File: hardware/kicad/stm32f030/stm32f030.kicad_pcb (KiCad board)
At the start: 2 copper layers, 72.4 x 50.2 mm, 91 parts, among them IC1 AT24CS02-SSHM, K1 RELAY_1RT, K2 RELAY_1RT, P1 5VIN, P10 SWD, P2 LOOP1, P3 LOOP2, P4 RELAY OUT 1, P5 TTL OUT 1, P6 RELAY OUT 2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

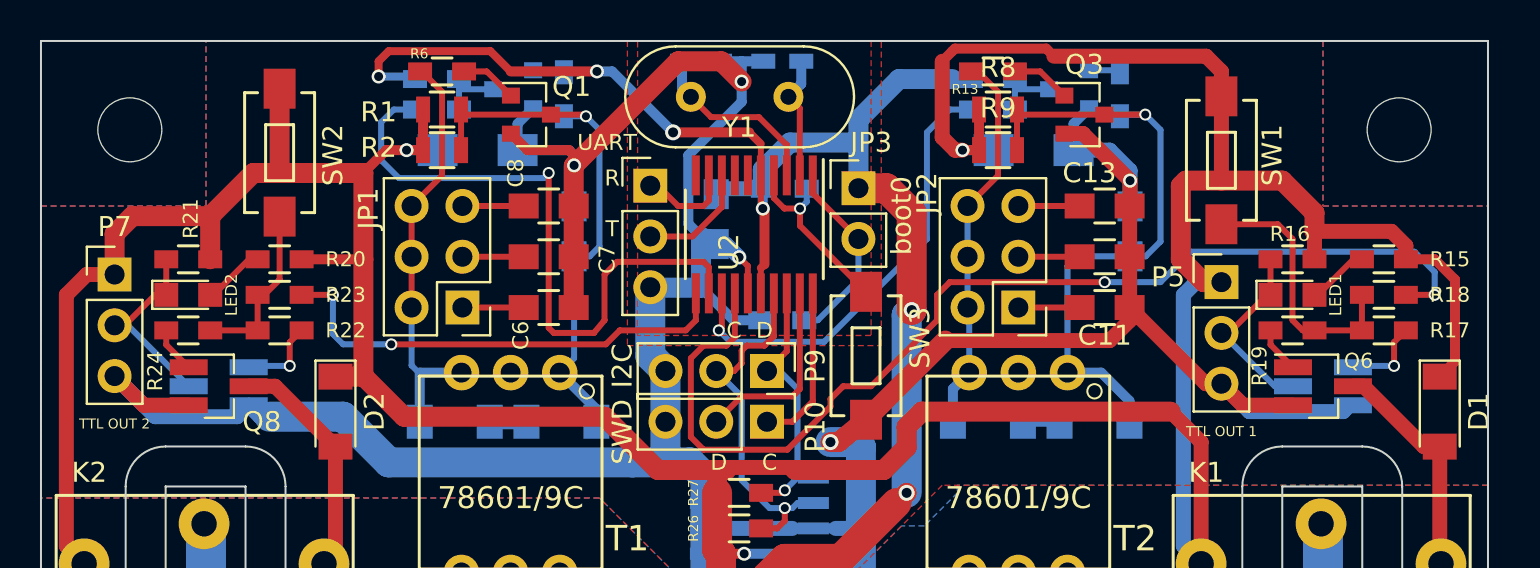
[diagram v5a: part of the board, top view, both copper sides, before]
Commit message: stm32f030 PCB text fixes
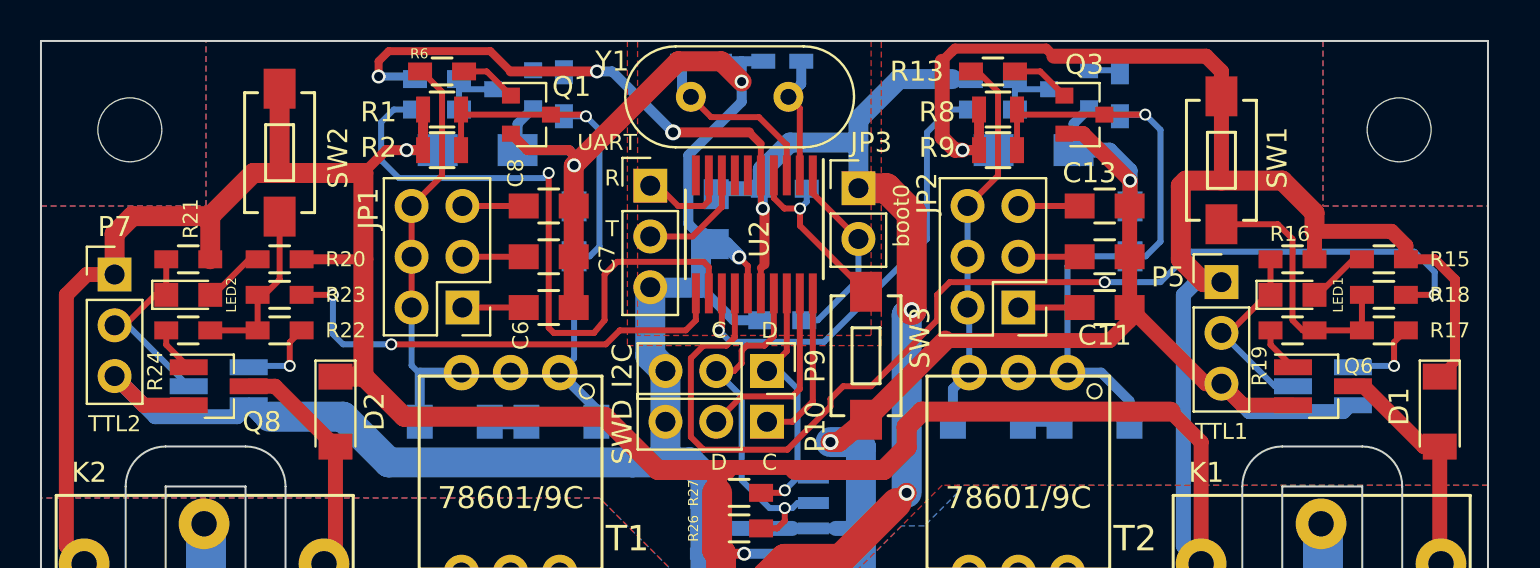
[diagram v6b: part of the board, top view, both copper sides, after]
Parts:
- P5: value TTL OUT 1 -> TTL1
- P7: value TTL OUT 2 -> TTL2
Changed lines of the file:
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@@
     (links 174)
     (no_connects 0)
-    (area 53.924999 112.979999 126.415001 163.245001)
+    (area 39.140001 103.98 131.527143 168.054001)
     (thickness 1.6)
     (drawings 40)
@@
     (46 B.CrtYd user)
     (47 F.CrtYd user)
-    (48 B.Fab user hide)
-    (49 F.Fab user hide)
+    (48 B.Fab user)
+    (49 F.Fab user)
   )
   (setup
@@
     (tags "capacitor 1206")
     (attr smd)
-    (fp_text reference C4 (at 1.397 1.905) (layer B.SilkS)
+    (fp_text reference C4 (at 1.905 2.159) (layer B.SilkS)
       (effects (font (size 1 1) (thickness 0.15)) (justify mirror))
     )
@@
     (tags "capacitor 0805")
     (attr smd)
-    (fp_text reference C5 (at 0.127 1.651 90) (layer B.SilkS)
+    (fp_text reference C5 (at 0.127 1.905 90) (layer B.SilkS)
       (effects (font (size 1 1) (thickness 0.15)) (justify mirror))
     )
@@
     (tags "capacitor 1206")
     (attr smd)
-    (fp_text reference C9 (at 1.016 1.905) (layer B.SilkS)
+    (fp_text reference C9 (at 1.778 2.159) (layer B.SilkS)
       (effects (font (size 1 1) (thickness 0.15)) (justify mirror))
     )
@@
     (tags "capacitor 0603")
     (attr smd)
-    (fp_text reference C14 (at -2.667 1.27) (layer B.SilkS)
+    (fp_text reference C14 (at -3.429 0.254) (layer B.SilkS)
       (effects (font (size 1 1) (thickness 0.15)) (justify mirror))
     )
@@
     (tags "capacitor 0603")
     (attr smd)
-    (fp_text reference C15 (at -2.921 -1.27 180) (layer B.SilkS)
+    (fp_text reference C15 (at -3.429 -0.254 180) (layer B.SilkS)
       (effects (font (size 1 1) (thickness 0.15)) (justify mirror))
     )
@@
     (tags "LED led 0805 SMD smd SMT smt smdled SMDLED smtled SMTLED")
     (attr smd)
-    (fp_text reference LED1 (at 2.159 0 90) (layer F.SilkS)
-      (effects (font (size 0.6 0.6) (thickness 0.1)))
+    (fp_text reference LED1 (at 2.286 0 90) (layer F.SilkS)
+      (effects (font (size 0.5 0.5) (thickness 0.08)))
     )
     (fp_text value LED_Small (at 0 1.55) (layer F.Fab) hide
@@
     (attr smd)
     (fp_text reference LED2 (at 2.159 0 90) (layer F.SilkS)
-      (effects (font (size 0.6 0.6) (thickness 0.1)))
+      (effects (font (size 0.5 0.5) (thickness 0.08)))
     )
     (fp_text value LED_Small (at 0 1.55) (layer F.Fab) hide
@@
     (tags "resistor 0603")
     (attr smd)
-    (fp_text reference R3 (at 0.127 -1.397) (layer B.SilkS)
-      (effects (font (size 0.5 0.5) (thickness 0.1)) (justify mirror))
+    (fp_text reference R3 (at -2.921 -0.127) (layer B.SilkS)
+      (effects (font (size 0.8 0.8) (thickness 0.1)) (justify mirror))
     )
     (fp_text value 1k (at -4.953 0) (layer B.Fab) hide
@@
     (tags "resistor 0603")
     (attr smd)
-    (fp_text reference R4 (at -2.667 -0.127) (layer B.SilkS)
-      (effects (font (size 0.5 0.5) (thickness 0.1)) (justify mirror))
+    (fp_text reference R4 (at -2.921 -0.127) (layer B.SilkS)
+      (effects (font (size 0.8 0.8) (thickness 0.1)) (justify mirror))
     )
     (fp_text value 4.7k (at -5.588 -0.127) (layer B.Fab) hide
@@
     (tags "resistor 0603")
     (attr smd)
-    (fp_text reference R5 (at -0.127 1.397 90) (layer B.SilkS)
+    (fp_text reference R5 (at -0.127 1.651 90) (layer B.SilkS)
       (effects (font (size 0.8 0.8) (thickness 0.1)) (justify mirror))
     )
@@
     (tags "resistor 0603")
     (attr smd)
-    (fp_text reference R10 (at -2.794 -0.127 180) (layer B.SilkS)
-      (effects (font (size 0.5 0.5) (thickness 0.1)) (justify mirror))
+    (fp_text reference R10 (at -3.302 -0.127) (layer B.SilkS)
+      (effects (font (size 0.8 0.8) (thickness 0.1)) (justify mirror))
     )
     (fp_text value 1k (at -5.715 0.127) (layer B.Fab) hide
@@
     (tags "resistor 0603")
     (attr smd)
-    (fp_text reference R11 (at -2.794 -0.127 180) (layer B.SilkS)
-      (effects (font (size 0.5 0.5) (thickness 0.1)) (justify mirror))
+    (fp_text reference R11 (at -3.302 -0.127) (layer B.SilkS)
+      (effects (font (size 0.8 0.8) (thickness 0.1)) (justify mirror))
     )
     (fp_text value 4.7k (at -6.223 0.254) (layer B.Fab) hide
@@
     (tags "resistor 0603")
     (attr smd)
-    (fp_text reference R12 (at 0.127 1.27 270) (layer B.SilkS)
-      (effects (font (size 0.5 0.5) (thickness 0.1)) (justify mirror))
+    (fp_text reference R12 (at 0.127 1.524 90) (layer B.SilkS)
+      (effects (font (size 0.8 0.8) (thickness 0.1)) (justify mirror))
     )
     (fp_text value 4.7k (at -6.223 0 90) (layer B.Fab) hide
@@
     (tags "resistor 0603")
     (attr smd)
-    (fp_text reference R13 (at 1.397 -0.889 360) (layer F.SilkS)
-      (effects (font (size 0.5 0.5) (thickness 0.1)))
+    (fp_text reference R13 (at 3.81 0 180) (layer F.SilkS)
+      (effects (font (size 1 1) (thickness 0.15)))
     )
     (fp_text value 1k (at 5.715 0 180) (layer F.Fab) hide
@@
     (tags "resistor 0603")
     (attr smd)
-    (fp_text reference R25 (at 2.286 -0.023 90) (layer B.SilkS)
-      (effects (font (size 0.5 0.5) (thickness 0.1)) (justify mirror))
+    (fp_text reference R25 (at 0 1.755) (layer B.SilkS)
+      (effects (font (size 0.8 0.8) (thickness 0.15)) (justify mirror))
     )
     (fp_text value 10k (at 0 -1.524) (layer B.Fab) hide
@@
       (effects (font (size 1 1) (thickness 0.15)))
     )
-    (fp_text value "TTL OUT 1" (at 0 7.47) (layer F.SilkS)
-      (effects (font (size 0.5 0.5) (thickness 0.06)))
+    (fp_text value TTL1 (at 0 7.47) (layer F.SilkS)
+      (effects (font (size 0.8 0.8) (thickness 0.1)))
     )
     (fp_line (start -1.27 -1.27) (end -1.27 6.35) (layer F.Fab) (width 0.1))
@@
       (effects (font (size 1 1) (thickness 0.15)))
     )
-    (fp_text value "TTL OUT 2" (at 0 7.47) (layer F.SilkS)
-      (effects (font (size 0.5 0.5) (thickness 0.06)))
+    (fp_text value TTL2 (at 0 7.47) (layer F.SilkS)
+      (effects (font (size 0.8 0.8) (thickness 0.1)))
     )
     (fp_line (start -1.27 -1.27) (end -1.27 6.35) (layer F.Fab) (width 0.1))
@@
     (tags SOT-23)
     (attr smd)
-    (fp_text reference Q5 (at -3.81 -0.254 180) (layer B.SilkS)
+    (fp_text reference Q5 (at -3.81 -0.508 180) (layer B.SilkS)
       (effects (font (size 1 1) (thickness 0.15)) (justify mirror))
     )
@@
     (tags SOT-23)
     (attr smd)
-    (fp_text reference Q6 (at 1.778 -1.27) (layer F.SilkS)
-      (effects (font (size 0.75 0.75) (thickness 0.14)))
+    (fp_text reference Q6 (at 1.778 -1.016) (layer F.SilkS)
+      (effects (font (size 0.75 0.75) (thickness 0.1)))
     )
     (fp_text value BC817-40 (at 0 2.5) (layer F.Fab) hide
@@
     (tags SOT-23)
     (attr smd)
-    (fp_text reference Q7 (at -3.937 -0.254 180) (layer B.SilkS)
+    (fp_text reference Q7 (at -3.937 -0.508 180) (layer B.SilkS)
       (effects (font (size 1 1) (thickness 0.15)) (justify mirror))
     )
@@
     (tags "resistor 0603")
     (attr smd)
-    (fp_text reference R28 (at -2.413 0 270) (layer B.SilkS)
-      (effects (font (size 0.5 0.5) (thickness 0.1)) (justify mirror))
+    (fp_text reference R28 (at -0.127 1.524 180) (layer B.SilkS)
+      (effects (font (size 0.8 0.8) (thickness 0.15)) (justify mirror))
     )
     (fp_text value 10k (at 0 -1.9 180) (layer B.Fab) hide
@@
     )
     (fp_text value boot0 (at 2.159 1.374 90) (layer F.SilkS)
-      (effects (font (size 1 1) (thickness 0.15)))
+      (effects (font (size 0.8 0.8) (thickness 0.15)))
     )
     (fp_line (start -1.27 -1.27) (end -1.27 3.81) (layer F.Fab) (width 0.1))
@@
     (tags "SSOP 0.65")
     (attr smd)
-    (fp_text reference U2 (at 0.889 1.27 270) (layer F.SilkS)
+    (fp_text reference U2 (at 0.231 -0.254 270) (layer F.SilkS)
       (effects (font (size 1 1) (thickness 0.15)))
     )
@@
     (tags "Diode Mini-MELF Standard")
     (attr smd)
-    (fp_text reference D1 (at 0 -1.95 270) (layer F.SilkS)
+    (fp_text reference D1 (at -0.254 2.032 270) (layer F.SilkS)
       (effects (font (size 1 1) (thickness 0.15)))
     )
@@
     (tags "resistor 0805")
     (attr smd)
-    (fp_text reference R8 (at 0 -2.1) (layer F.SilkS)
+    (fp_text reference R8 (at -3.048 0.127) (layer F.SilkS)
       (effects (font (size 1 1) (thickness 0.15)))
     )
@@
     (tags "resistor 0805")
     (attr smd)
-    (fp_text reference R9 (at 0 -2.1) (layer F.SilkS)
+    (fp_text reference R9 (at -3.048 -0.127) (layer F.SilkS)
       (effects (font (size 1 1) (thickness 0.15)))
     )
@@
     (descr "Crystal THT HC-49-4H http://5hertz.com/pdfs/04404_D.pdf")
     (tags "THT crystalHC-49-4H")
-    (fp_text reference Y1 (at 2.413 1.524) (layer F.SilkS)
+    (fp_text reference Y1 (at -3.937 -1.778) (layer F.SilkS)
       (effects (font (size 1 1) (thickness 0.15)))
     )
@@
     (descr "Light Touch Switch")
     (attr smd)
-    (fp_text reference SW1 (at -0.254 -2.54 270) (layer F.SilkS)
+    (fp_text reference SW1 (at -0.127 -2.794 270) (layer F.SilkS)
       (effects (font (size 1 1) (thickness 0.15)))
     )
@@
     (descr "Light Touch Switch")
     (attr smd)
-    (fp_text reference SW2 (at 0.127 -2.667 270) (layer F.SilkS)
+    (fp_text reference SW2 (at 0.254 -2.921 270) (layer F.SilkS)
       (effects (font (size 1 1) (thickness 0.15)))
     )
@@
     (effects (font (size 0.8 0.8) (thickness 0.1)))
   )
-  (gr_text D (at 90.17 127.508) (layer F.SilkS)
+  (gr_text D (at 90.424 127.508) (layer F.SilkS)
     (effects (font (size 0.8 0.8) (thickness 0.1)))
   )
-  (gr_text C (at 88.646 127.508) (layer F.SilkS)
+  (gr_text C (at 87.884 127.508) (layer F.SilkS)
     (effects (font (size 0.8 0.8) (thickness 0.1)))
   )

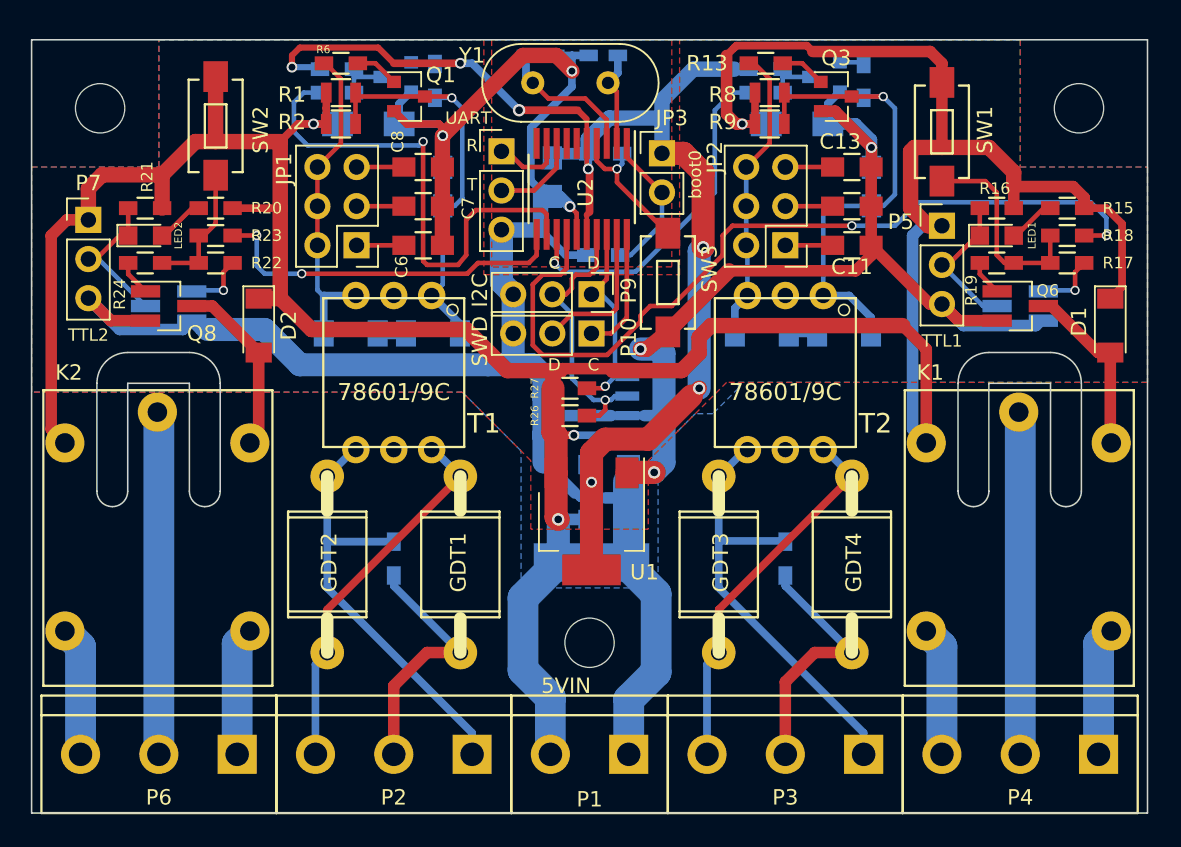
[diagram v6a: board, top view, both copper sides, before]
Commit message: kicad/stm32f030: corrected board size
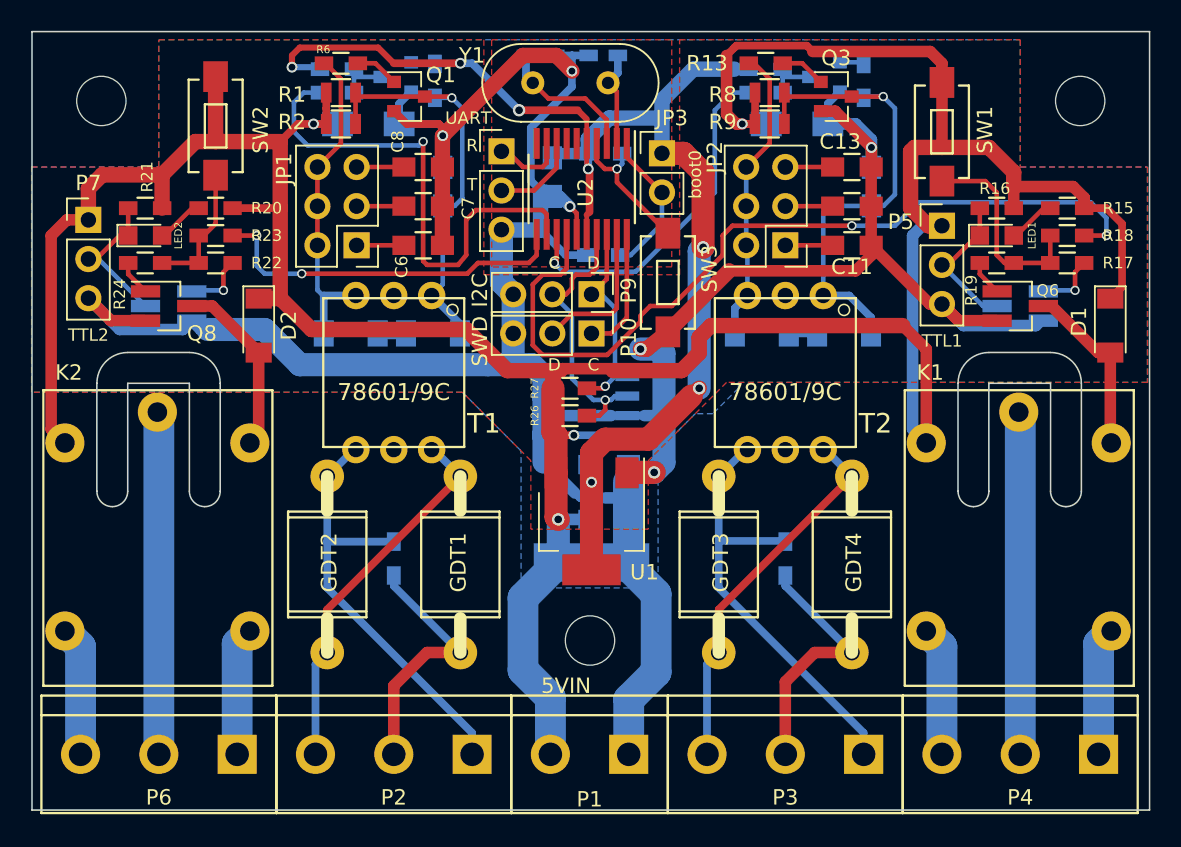
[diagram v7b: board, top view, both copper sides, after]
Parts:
- moved REF** 0.48 mm to (122.0, 117.0)
- moved REF** 0.48 mm to (58.5, 117.0)
- moved REF** 0.15 mm to (90.2, 152.0)
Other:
- board size 72.4 x 50.2 mm -> 72.5 x 50.5 mm

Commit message: kicad-STM32F030 modifications during test batch assembly
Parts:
- C10, C5: footprint Capacitors_SMD:C_0805_HandSoldering -> Capacitors_SMD:C_1206_HandSoldering
- C11, C6: footprint Capacitors_SMD:C_0805_HandSoldering -> Capacitors_SMD:C_1206
- P5: value TTL1 -> TTL OUT 1
- P7: value TTL2 -> TTL OUT 2
- U1: footprint TO_SOT_Packages_SMD:SOT-223 -> TO_SOT_Packages_SMD:SOT-223-3Lead_TabPin2
